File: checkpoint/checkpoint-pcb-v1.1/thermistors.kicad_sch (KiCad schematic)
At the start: 39 parts, among them J1 T0, J2 T1, J3 T2, J4 T3, J5 2_WIRE, J6 24_3_WIRE_A, J7 PT100, J8 23_WIRE, J9 PT100_1K, U1 MAX31865xTP

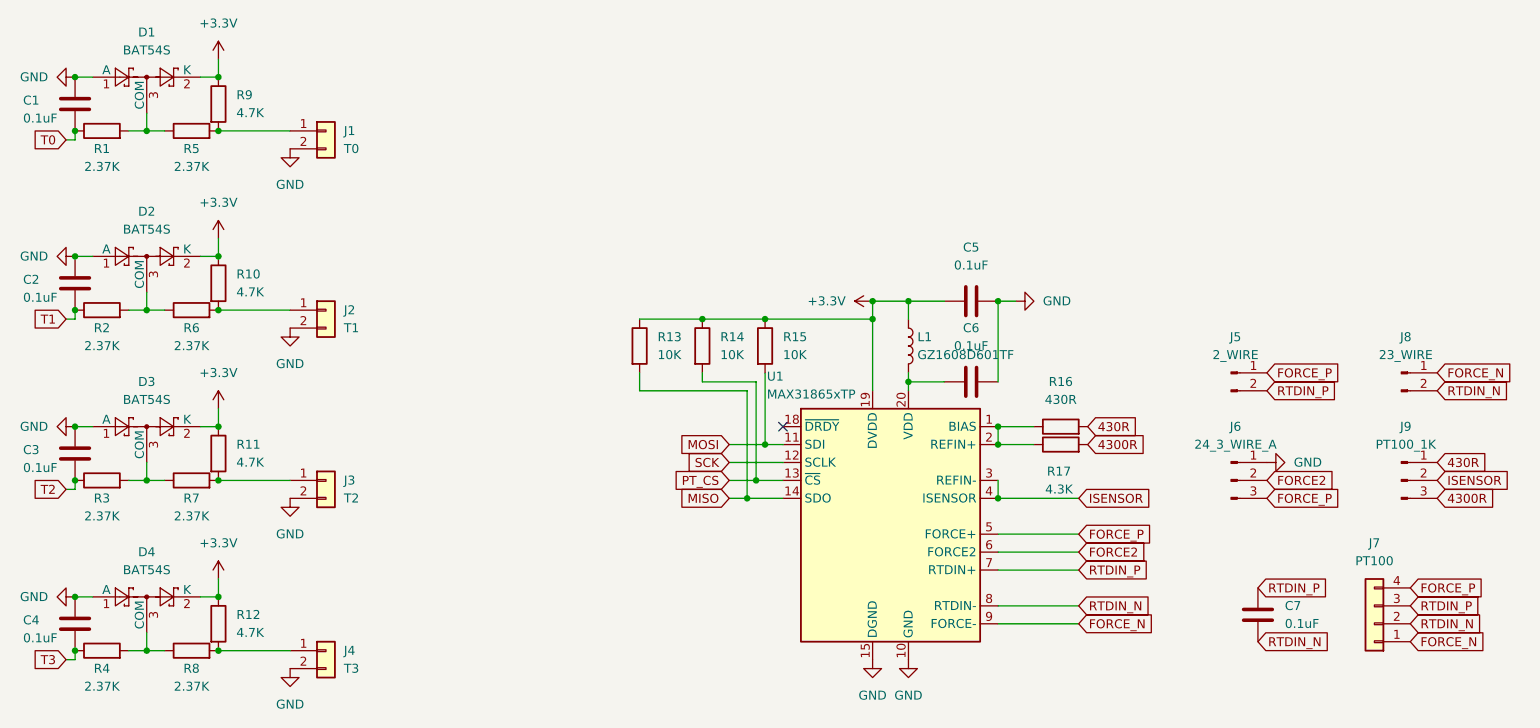
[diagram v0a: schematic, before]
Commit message: chore: update component rotation
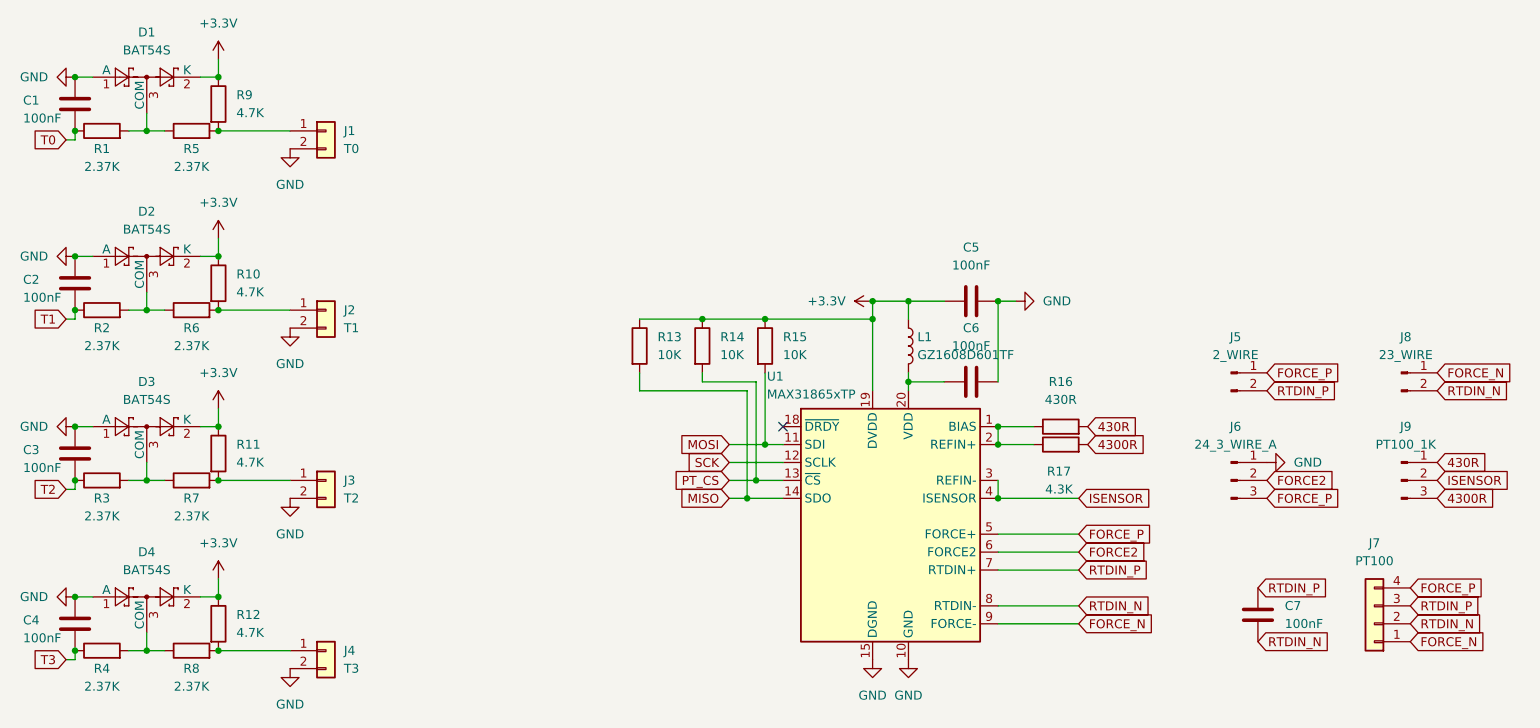
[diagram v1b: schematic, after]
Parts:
- C1, C2, C3, C4, C5, C6, C7: value 0.1uF -> 100nF
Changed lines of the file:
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@@
 			)
 		)
-		(property "Value" "0.1uF"
+		(property "Value" "100nF"
 			(at 220.98 119.3799 0)
 			(effects
@@
 			)
 		)
-		(property "Value" "0.1uF"
+		(property "Value" "100nF"
 			(at 42.164 97.282 0)
 			(effects
@@
 			)
 		)
-		(property "Value" "0.1uF"
+		(property "Value" "100nF"
 			(at 42.164 121.412 0)
 			(effects
@@
 			)
 		)
-		(property "Value" "0.1uF"
+		(property "Value" "100nF"
 			(at 42.164 47.752 0)
 			(effects
@@
 			)
 		)
-		(property "Value" "0.1uF"
+		(property "Value" "100nF"
 			(at 176.53 68.58 90)
 			(effects
@@
 			)
 		)
-		(property "Value" "0.1uF"
+		(property "Value" "100nF"
 			(at 176.53 80.01 90)
 			(effects
@@
 			)
 		)
-		(property "Value" "0.1uF"
+		(property "Value" "100nF"
 			(at 42.164 73.152 0)
 			(effects
